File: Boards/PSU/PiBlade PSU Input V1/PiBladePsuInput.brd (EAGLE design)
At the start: 85 x 56 mm, 35 parts, among them J1 CONN_20X2NOSILK, Q1 220mA/50V/3.5Ω, Q2 220mA/50V/3.5Ω, Q3 220mA/50V/3.5Ω, U1 INA219AIDCNRSOIC, U2 R-78E5.0-1.0, U4 Tiny85-20-SMT

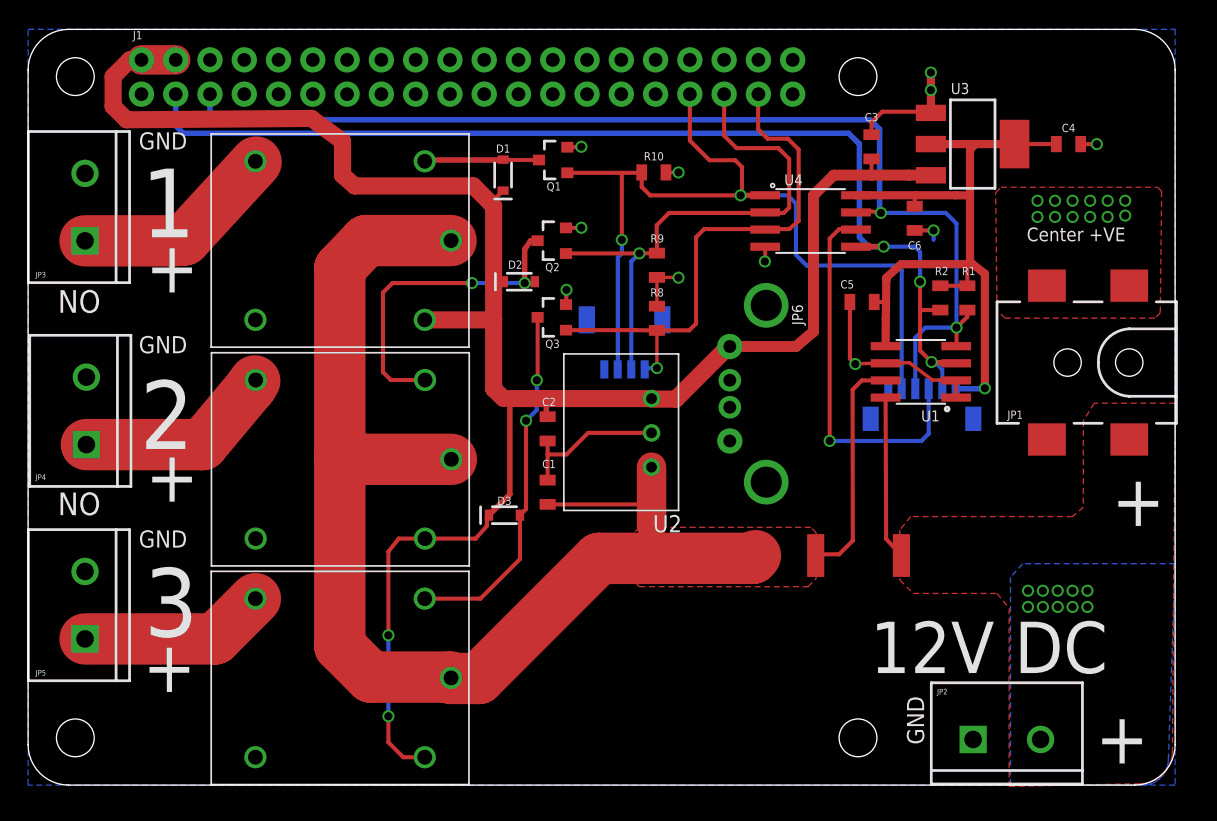
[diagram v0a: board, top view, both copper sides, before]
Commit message: Update PSU input board: * Added LEDs. * Moved DC Jack input to a lower position to align with the USB board better.
Updated DirtyPCBs
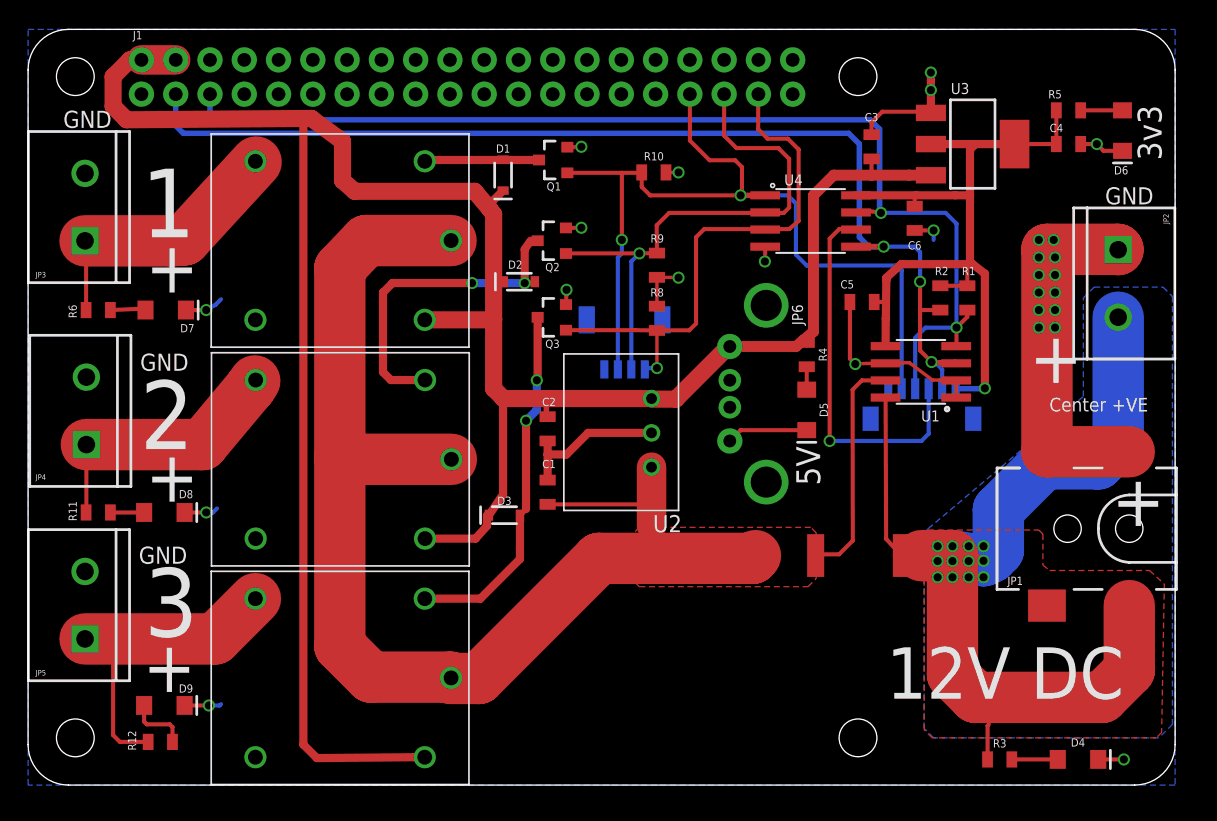
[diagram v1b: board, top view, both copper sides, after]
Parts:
- added D4, D5, D6, D7, D8, D9: BLUE, SparkFun-LED:LED-1206
- added R11, R12, R3, R4, R5, R6: (no value), SparkFun-Resistors:0805
- moved JP2 37.8 mm to (80.8, 39.7), turned to 270 degrees
- moved JP1 12.3 mm to (81.6, 19.0)
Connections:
- new net N$1: D4.A, R3.2
- new net N$2: D6.A, R5.2
- new net N$3: D7.A, R6.2
- new net N$4: D5.A, R4.2
- new net N$5: D8.A, R11.2
- new net N$6: D9.A, R12.2
- net 3.3V: now also R5.1
- net 5V: now also R4.1
- net GND: now also D4.C, D5.C, D6.C, D7.C, D8.C, D9.C
- net OUT1: now also R6.1
- net OUT2: now also R11.1
- net OUT3: now also R12.1
- net VIN: now also R3.1
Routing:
- net VIN: track 12.1 -> 85.8 mm, vias 10 -> 12
- net GND: track 46.6 -> 91.2 mm, vias 23 -> 27
- net 5V: track 144.5 -> 180.3 mm, vias 2 -> 0
- net OUT3: track 13.9 -> 25.4 mm
- net OUT1: track 15.3 -> 20.5 mm
- net OUT2: track 14.8 -> 19.8 mm
- net N$6: track 0.00 -> 4.57 mm
- net N$1: track 0.00 -> 3.40 mm
- net N$2: track 0.00 -> 3.10 mm
- net N$3: track 0.00 -> 2.63 mm
- net N$5: track 0.00 -> 2.50 mm
- net 3.3V: track 55.9 -> 58.4 mm
- net N$4: track 0.00 -> 1.70 mm
- removed copper zone on layer 1, net GND
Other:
- board text added: "3v3"
- board text added: "5V"
- board text removed: "NO"
